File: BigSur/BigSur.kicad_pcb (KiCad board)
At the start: 2 copper layers, 200 x 70 mm, 152 parts, among them J1 XT30PW-M, J10 XT30PW-M, J12 XT30PW-M, J14 XT30PW-M, J15 XT30PW-M, J16 XT30PW-M, J2 XT30PW-M, J3 XT30PW-M, J4 XT30PW-M, J5 XT30PW-M, J6 XT30PW-M, J7 XT30PW-M, J8 XT30PW-M, J9 XT30PW-M, K1 G5LE-1A-VDDC12, K2 G5LE-1A-VDDC12, K3 G5LE-1A-VDDC12, K4 G5LE-1A-VDDC12, Q1 TSM900N10, Q2 TSM900N10, Q3 MMBT3904-7-F, Q4 MMBT3904-7-F, Q5 MMBT3904-7-F, Q6 MMBT3904-7-F, U1 DRV103H, U10 MCP6L02T-E_MS, U11 74LVC1G00W5-7, U12 ACS70331EESATR-2P5U3, U2 DRV103H, U3 DRV8806, U4 SMD46, U5 ACS70331EESATR-2P5U3, U6 ACS70331EESATR-2P5U3, U7 ACS70331EESATR-2P5U3, U8 ACS70331EESATR-2P5U3, U9 ACS70331EESATR-2P5U3

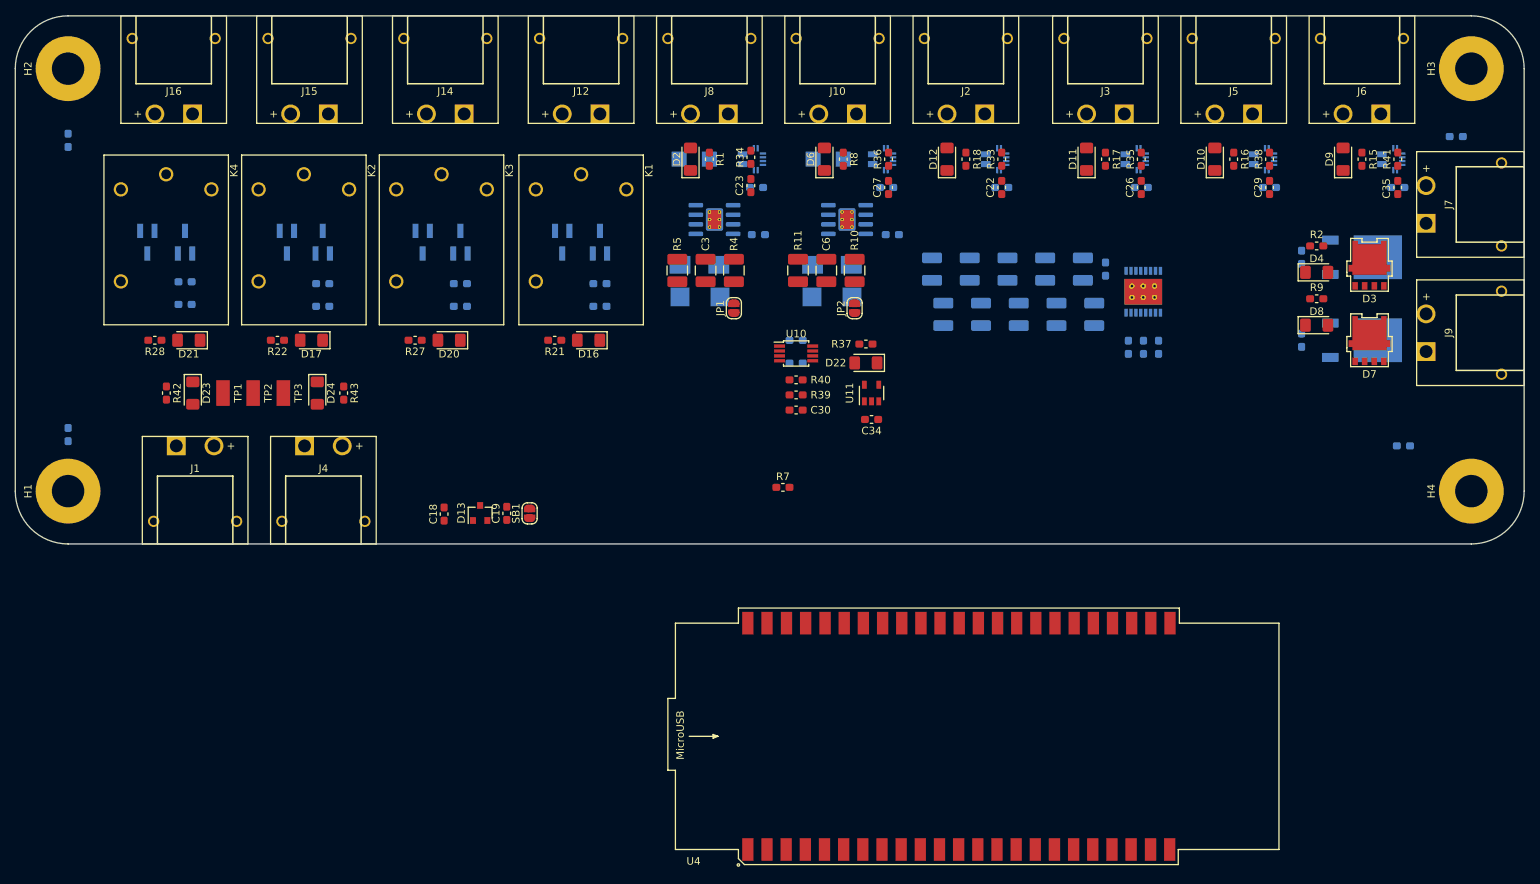
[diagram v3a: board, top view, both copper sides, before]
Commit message: Squished output connectors together, going to need to fix layout.
Also still needs CAN and inverter chill connectors.
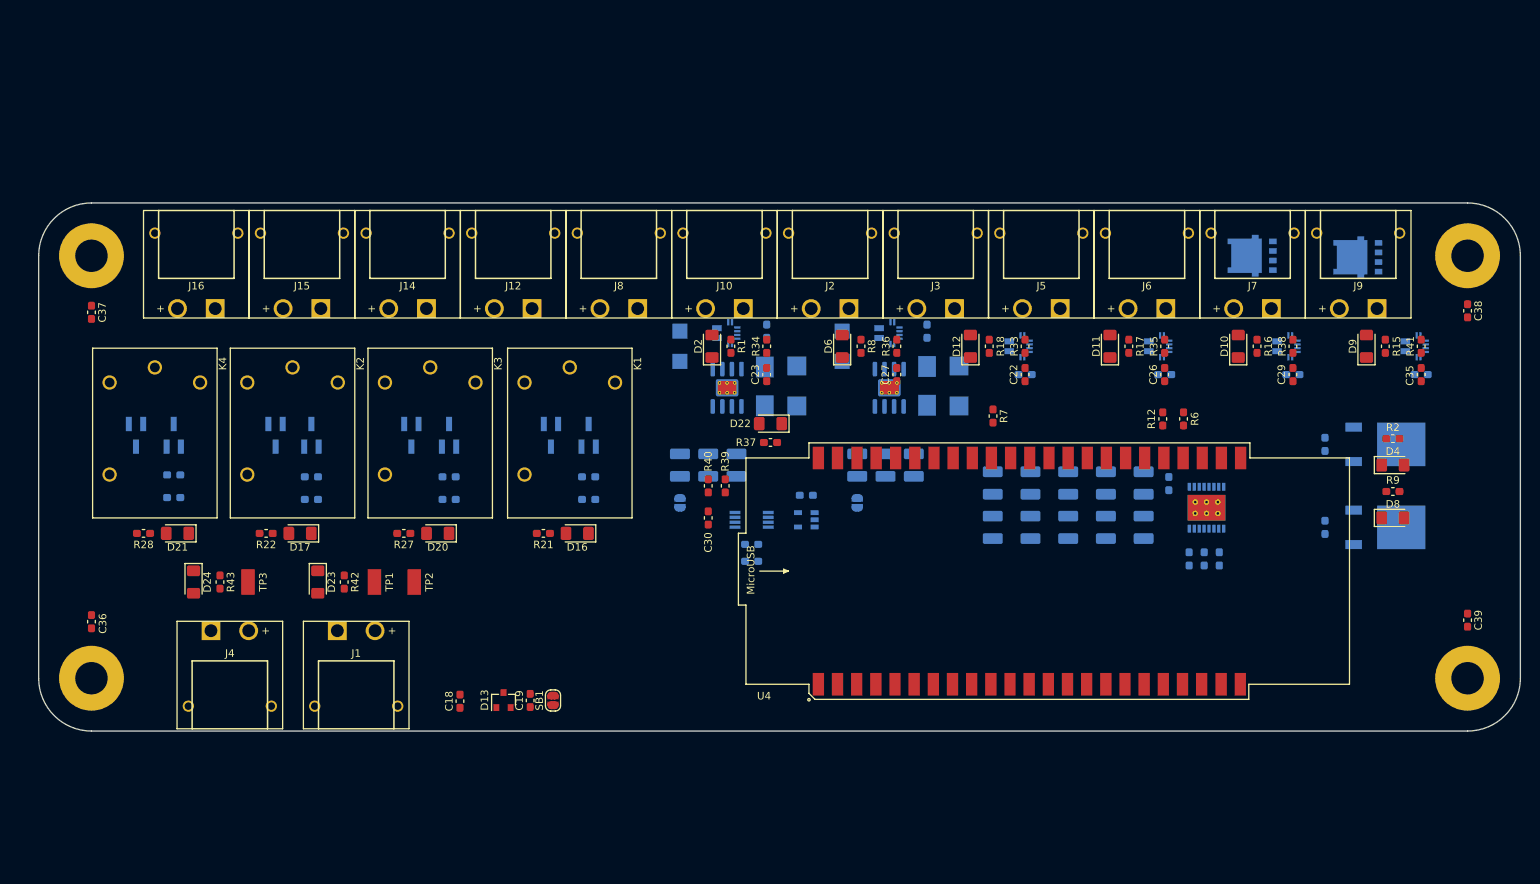
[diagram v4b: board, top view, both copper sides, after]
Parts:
- C3, C34, C6, D3, D7, JP1, JP2, R10, R11, R4, R5, U10, U11: moved to B.Cu
- C36, C37, C38, C39, R12, R6: moved to F.Cu
- moved R6 61.4 mm to (199.8, 83.4), turned to 90 degrees
- moved R12 43.4 mm to (197.1, 83.4), turned to 90 degrees
- moved J6 38.4 mm to (195.0, 58.8)
- moved J5 36.3 mm to (181.0, 58.8)
- moved R42 34.4 mm to (88.6, 105.0)
- moved J3 34.2 mm to (167.0, 58.8)
- moved J7 33.2 mm to (209.0, 58.8), turned to 0 degrees
- moved TP2 32.9 mm to (97.9, 105.0)
- moved J1 32.5 mm to (90.2, 121.5)
- moved TP1 32.1 mm to (92.6, 105.0)
- moved J2 31.5 mm to (153.0, 58.8)
- moved D23 30.0 mm to (85.1, 105.0)
- moved D24 29.9 mm to (68.6, 105.0)
- moved R43 29.9 mm to (72.1, 105.0)
- moved C32 29.9 mm to (142.6, 102.3)
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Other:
- board size 200 x 70 mm -> 196.4 x 70 mm

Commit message: More layout changes
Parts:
- moved C3 130.3 mm to (266.4, 103.5)
- moved C30 130.3 mm to (266.4, 110.5)
- moved C32 130.3 mm to (272.1, 116.3)
- moved C33 130.3 mm to (272.1, 114.0)
- moved C34 130.3 mm to (279.4, 107.5)
- moved C6 130.3 mm to (289.9, 103.5)
- moved D22 130.3 mm to (274.6, 98.0)
- moved JP1 130.3 mm to (262.6, 108.5)
- moved JP2 130.3 mm to (286.1, 108.5)
- moved R10 130.3 mm to (293.6, 103.5)
- moved R11 130.3 mm to (286.1, 103.5)
- moved R37 130.3 mm to (274.6, 100.5)
- moved R39 130.3 mm to (268.6, 106.3)
- moved R4 130.3 mm to (270.1, 103.5)
- moved R40 130.3 mm to (266.4, 106.3)
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
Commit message: Fixed braking LED direction
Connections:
- D22 pad 1: BRAKE_SOLENOID_LOW -> GND
- R37 pad 1: +3V3 -> BRAKE_SOLENOID_HIGH
- U11 pad 4: BRAKE_SOLENOID_LOW -> BRAKE_SOLENOID_HIGH

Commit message: Finished another layout pass.
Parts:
- added G***: LOGO, Silkscreen:j_logo, F.Cu at (234.2, 77.8)
- C22, C26, C29, C30, R33, R35, R38, R39, R40: moved to B.Cu
- moved C10 185.2 mm to (124.1, 98.4)
- moved C11 185.2 mm to (119.1, 98.4)
- moved C12 185.2 mm to (139.1, 104.3)
- moved C13 185.2 mm to (134.1, 104.3)
- moved C14 185.2 mm to (129.1, 104.3)
- moved C15 185.2 mm to (124.1, 104.3)
- moved C16 185.2 mm to (119.1, 104.3)
- moved C7 185.2 mm to (139.1, 98.4)
- moved C8 185.2 mm to (134.1, 98.4)
- moved C9 185.2 mm to (129.1, 98.4)
- moved C17 185.2 mm to (142.4, 98.5)
- moved U3 185.2 mm to (147.4, 101.7)
- moved R19 165.6 mm to (168.5, 113.8), turned to 270 degrees
- moved R14 161.4 mm to (170.8, 113.8)
- moved R20 149.1 mm to (181.0, 113.8), turned to 270 degrees
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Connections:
- U4 pad 31: DRV8806_SERIAL_DATOUT -> DRV8806_SERIAL_DATOUT_3.3V
- U4 pad 36: DRV8806_SERIAL_DATOUT_3.3V -> Net-(U4-Pad36)
